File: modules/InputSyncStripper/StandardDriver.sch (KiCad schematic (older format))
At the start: 10 parts

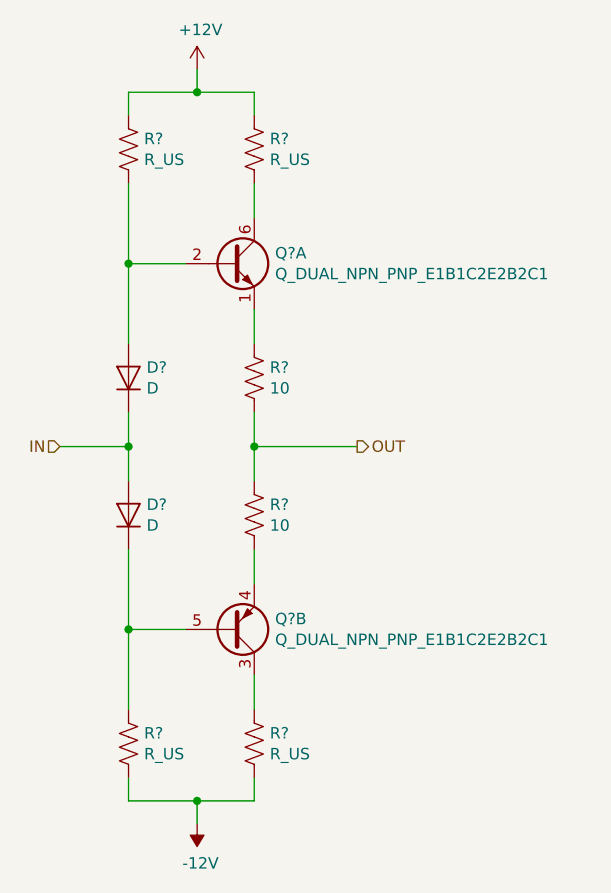
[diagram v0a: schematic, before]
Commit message: fix some ERC issues; assign symbols
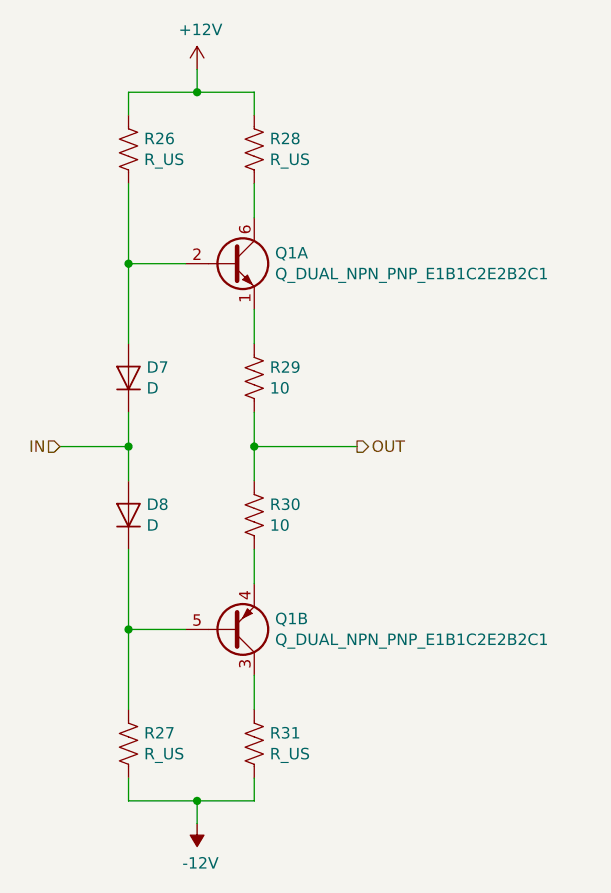
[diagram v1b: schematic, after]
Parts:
- gave numbers to parts that had none: 9
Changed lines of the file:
@@
 EESchema Schematic File Version 4
-LIBS:SIP-cache
+LIBS:InputSyncStripper-cache
 EELAYER 26 0
 EELAYER END
 $Descr A 11000 8500
 encoding utf-8
-Sheet 3 10
+Sheet 9 10
 Title "Sandin Image Processor/Standard Driver"
 Date ""
@@
 OUT
 $Comp
-L Device:D D?
+L Device:D D7
 U 1 1 5BC9A4E0
 P 3950 3450
-AR Path="/5BC7EA60/5BC8D7ED/5BC9A4E0" Ref="D?"  Part="1"
-AR Path="/5BC9C4B4/5BCA0111/5BC9A4E0" Ref="D?"  Part="1"
-AR Path="/5BCA510D/5BCA535E/5BC9A4E0" Ref="D?"  Part="1"
-AR Path="/5BCA5116/5BCAE8EB/5BC9A4E0" Ref="D?"  Part="1"
-F 0 "D?" V 3996 3371 50  0000 R CNN
+AR Path="/5BC7EA60/5BC8D7ED/5BC9A4E0" Ref="D7"  Part="1"
+AR Path="/5BC9C4B4/5BCA0111/5BC9A4E0" Ref="D10"  Part="1"
+AR Path="/5BCA510D/5BCA535E/5BC9A4E0" Ref="D13"  Part="1"
+AR Path="/5BCA5116/5BCAE8EB/5BC9A4E0" Ref="D17"  Part="1"
+F 0 "D7" V 3996 3371 50  0000 R CNN
 F 1 "D" V 3905 3371 50  0000 R CNN
 F 2 "" H 3950 3450 50  0001 C CNN
@@
 $EndComp
 $Comp
-L Device:D D?
+L Device:D D8
 U 1 1 5BC9A54B
 P 3950 4050
-AR Path="/5BC7EA60/5BC8D7ED/5BC9A54B" Ref="D?"  Part="1"
-AR Path="/5BC9C4B4/5BCA0111/5BC9A54B" Ref="D?"  Part="1"
-AR Path="/5BCA510D/5BCA535E/5BC9A54B" Ref="D?"  Part="1"
-AR Path="/5BCA5116/5BCAE8EB/5BC9A54B" Ref="D?"  Part="1"
-F 0 "D?" V 3996 3971 50  0000 R CNN
+AR Path="/5BC7EA60/5BC8D7ED/5BC9A54B" Ref="D8"  Part="1"
+AR Path="/5BC9C4B4/5BCA0111/5BC9A54B" Ref="D11"  Part="1"
+AR Path="/5BCA510D/5BCA535E/5BC9A54B" Ref="D14"  Part="1"
+AR Path="/5BCA5116/5BCAE8EB/5BC9A54B" Ref="D18"  Part="1"
+F 0 "D8" V 3996 3971 50  0000 R CNN
 F 1 "D" V 3905 3971 50  0000 R CNN
 F 2 "" H 3950 4050 50  0001 C CNN
@@
 $EndComp
 $Comp
-L Device:R_US R?
+L Device:R_US R30
 U 1 1 5BC9A59F
 P 4500 4050
-AR Path="/5BC7EA60/5BC8D7ED/5BC9A59F" Ref="R?"  Part="1"
-AR Path="/5BC9C4B4/5BCA0111/5BC9A59F" Ref="R?"  Part="1"
-AR Path="/5BCA510D/5BCA535E/5BC9A59F" Ref="R?"  Part="1"
-AR Path="/5BCA5116/5BCAE8EB/5BC9A59F" Ref="R?"  Part="1"
-F 0 "R?" H 4568 4096 50  0000 L CNN
+AR Path="/5BC7EA60/5BC8D7ED/5BC9A59F" Ref="R30"  Part="1"
+AR Path="/5BC9C4B4/5BCA0111/5BC9A59F" Ref="R41"  Part="1"
+AR Path="/5BCA510D/5BCA535E/5BC9A59F" Ref="R53"  Part="1"
+AR Path="/5BCA5116/5BCAE8EB/5BC9A59F" Ref="R63"  Part="1"
+F 0 "R30" H 4568 4096 50  0000 L CNN
 F 1 "10" H 4568 4005 50  0000 L CNN
 F 2 "" V 4540 4040 50  0001 C CNN
@@
 $EndComp
 $Comp
-L Device:R_US R?
+L Device:R_US R29
 U 1 1 5BC9A608
 P 4500 3450
-AR Path="/5BC7EA60/5BC8D7ED/5BC9A608" Ref="R?"  Part="1"
-AR Path="/5BC9C4B4/5BCA0111/5BC9A608" Ref="R?"  Part="1"
-AR Path="/5BCA510D/5BCA535E/5BC9A608" Ref="R?"  Part="1"
-AR Path="/5BCA5116/5BCAE8EB/5BC9A608" Ref="R?"  Part="1"
-F 0 "R?" H 4568 3496 50  0000 L CNN
+AR Path="/5BC7EA60/5BC8D7ED/5BC9A608" Ref="R29"  Part="1"
+AR Path="/5BC9C4B4/5BCA0111/5BC9A608" Ref="R40"  Part="1"
+AR Path="/5BCA510D/5BCA535E/5BC9A608" Ref="R52"  Part="1"
+AR Path="/5BCA5116/5BCAE8EB/5BC9A608" Ref="R62"  Part="1"
+F 0 "R29" H 4568 3496 50  0000 L CNN
 F 1 "10" H 4568 3405 50  0000 L CNN
 F 2 "" V 4540 3440 50  0001 C CNN
@@
 $EndComp
 $Comp
-L Device:Q_DUAL_NPN_PNP_E1B1C2E2B2C1 Q?
+L Device:Q_DUAL_NPN_PNP_E1B1C2E2B2C1 Q1
 U 1 1 5BC9A901
 P 4400 2950
-AR Path="/5BC7EA60/5BC8D7ED/5BC9A901" Ref="Q?"  Part="1"
-AR Path="/5BC9C4B4/5BCA0111/5BC9A901" Ref="Q?"  Part="1"
-AR Path="/5BCA510D/5BCA535E/5BC9A901" Ref="Q?"  Part="1"
-AR Path="/5BCA5116/5BCAE8EB/5BC9A901" Ref="Q?"  Part="1"
-F 0 "Q?" H 4591 2996 50  0000 L CNN
+AR Path="/5BC7EA60/5BC8D7ED/5BC9A901" Ref="Q1"  Part="1"
+AR Path="/5BC9C4B4/5BCA0111/5BC9A901" Ref="Q2"  Part="1"
+AR Path="/5BCA510D/5BCA535E/5BC9A901" Ref="Q3"  Part="1"
+AR Path="/5BCA5116/5BCAE8EB/5BC9A901" Ref="Q4"  Part="1"
+F 0 "Q1" H 4591 2996 50  0000 L CNN
 F 1 "Q_DUAL_NPN_PNP_E1B1C2E2B2C1" H 4591 2905 50  0000 L CNN
 F 2 "" H 4600 3050 50  0001 C CNN
@@
 $EndComp
 $Comp
-L Device:Q_DUAL_NPN_PNP_E1B1C2E2B2C1 Q?
+L Device:Q_DUAL_NPN_PNP_E1B1C2E2B2C1 Q1
 U 2 1 5BC9A9AF
 P 4400 4550
-AR Path="/5BC7EA60/5BC8D7ED/5BC9A9AF" Ref="Q?"  Part="2"
-AR Path="/5BC9C4B4/5BCA0111/5BC9A9AF" Ref="Q?"  Part="2"
-AR Path="/5BCA510D/5BCA535E/5BC9A9AF" Ref="Q?"  Part="2"
-AR Path="/5BCA5116/5BCAE8EB/5BC9A9AF" Ref="Q?"  Part="2"
-F 0 "Q?" H 4591 4504 50  0000 L CNN
+AR Path="/5BC7EA60/5BC8D7ED/5BC9A9AF" Ref="Q1"  Part="2"
+AR Path="/5BC9C4B4/5BCA0111/5BC9A9AF" Ref="Q2"  Part="2"
+AR Path="/5BCA510D/5BCA535E/5BC9A9AF" Ref="Q3"  Part="2"
+AR Path="/5BCA5116/5BCAE8EB/5BC9A9AF" Ref="Q4"  Part="2"
+F 0 "Q1" H 4591 4504 50  0000 L CNN
 F 1 "Q_DUAL_NPN_PNP_E1B1C2E2B2C1" H 4591 4595 50  0000 L CNN
 F 2 "" H 4600 4650 50  0001 C CNN
@@
 	3950 4550 4200 4550
 $Comp
-L Device:R_US R?
+L Device:R_US R31
 U 1 1 5BC9AC77
 P 4500 5050
-AR Path="/5BC7EA60/5BC8D7ED/5BC9AC77" Ref="R?"  Part="1"
-AR Path="/5BC9C4B4/5BCA0111/5BC9AC77" Ref="R?"  Part="1"
-AR Path="/5BCA510D/5BCA535E/5BC9AC77" Ref="R?"  Part="1"
-AR Path="/5BCA5116/5BCAE8EB/5BC9AC77" Ref="R?"  Part="1"
-F 0 "R?" H 4568 5096 50  0000 L CNN
+AR Path="/5BC7EA60/5BC8D7ED/5BC9AC77" Ref="R31"  Part="1"
+AR Path="/5BC9C4B4/5BCA0111/5BC9AC77" Ref="R42"  Part="1"
+AR Path="/5BCA510D/5BCA535E/5BC9AC77" Ref="R54"  Part="1"
+AR Path="/5BCA5116/5BCAE8EB/5BC9AC77" Ref="R64"  Part="1"
+F 0 "R31" H 4568 5096 50  0000 L CNN
 F 1 "R_US" H 4568 5005 50  0000 L CNN
 F 2 "" V 4540 5040 50  0001 C CNN
@@
 $EndComp
 $Comp
-L Device:R_US R?
+L Device:R_US R28
 U 1 1 5BC9ACDA
 P 4500 2450
-AR Path="/5BC7EA60/5BC8D7ED/5BC9ACDA" Ref="R?"  Part="1"
-AR Path="/5BC9C4B4/5BCA0111/5BC9ACDA" Ref="R?"  Part="1"
-AR Path="/5BCA510D/5BCA535E/5BC9ACDA" Ref="R?"  Part="1"
-AR Path="/5BCA5116/5BCAE8EB/5BC9ACDA" Ref="R?"  Part="1"
-F 0 "R?" H 4568 2496 50  0000 L CNN
+AR Path="/5BC7EA60/5BC8D7ED/5BC9ACDA" Ref="R28"  Part="1"
+AR Path="/5BC9C4B4/5BCA0111/5BC9ACDA" Ref="R39"  Part="1"
+AR Path="/5BCA510D/5BCA535E/5BC9ACDA" Ref="R51"  Part="1"
+AR Path="/5BCA5116/5BCAE8EB/5BC9ACDA" Ref="R61"  Part="1"
+F 0 "R28" H 4568 2496 50  0000 L CNN
 F 1 "R_US" H 4568 2405 50  0000 L CNN
 F 2 "" V 4540 2440 50  0001 C CNN
@@
 $EndComp
 $Comp
-L Device:R_US R?
+L Device:R_US R26
 U 1 1 5BC9AD46
 P 3950 2450
-AR Path="/5BC7EA60/5BC8D7ED/5BC9AD46" Ref="R?"  Part="1"
-AR Path="/5BC9C4B4/5BCA0111/5BC9AD46" Ref="R?"  Part="1"
-AR Path="/5BCA510D/5BCA535E/5BC9AD46" Ref="R?"  Part="1"
-AR Path="/5BCA5116/5BCAE8EB/5BC9AD46" Ref="R?"  Part="1"
-F 0 "R?" H 4018 2496 50  0000 L CNN
+AR Path="/5BC7EA60/5BC8D7ED/5BC9AD46" Ref="R26"  Part="1"
+AR Path="/5BC9C4B4/5BCA0111/5BC9AD46" Ref="R37"  Part="1"
+AR Path="/5BCA510D/5BCA535E/5BC9AD46" Ref="R49"  Part="1"
+AR Path="/5BCA5116/5BCAE8EB/5BC9AD46" Ref="R59"  Part="1"
+F 0 "R26" H 4018 2496 50  0000 L CNN
 F 1 "R_US" H 4018 2405 50  0000 L CNN
 F 2 "" V 3990 2440 50  0001 C CNN
@@
 $EndComp
 $Comp
-L Device:R_US R?
+L Device:R_US R27
 U 1 1 5BC9AD89
 P 3950 5050
-AR Path="/5BC7EA60/5BC8D7ED/5BC9AD89" Ref="R?"  Part="1"
-AR Path="/5BC9C4B4/5BCA0111/5BC9AD89" Ref="R?"  Part="1"
-AR Path="/5BCA510D/5BCA535E/5BC9AD89" Ref="R?"  Part="1"
-AR Path="/5BCA5116/5BCAE8EB/5BC9AD89" Ref="R?"  Part="1"
-F 0 "R?" H 4018 5096 50  0000 L CNN
+AR Path="/5BC7EA60/5BC8D7ED/5BC9AD89" Ref="R27"  Part="1"
+AR Path="/5BC9C4B4/5BCA0111/5BC9AD89" Ref="R38"  Part="1"
+AR Path="/5BCA510D/5BCA535E/5BC9AD89" Ref="R50"  Part="1"
+AR Path="/5BCA5116/5BCAE8EB/5BC9AD89" Ref="R60"  Part="1"
+F 0 "R27" H 4018 5096 50  0000 L CNN
 F 1 "R_US" H 4018 5005 50  0000 L CNN
 F 2 "" V 3990 5040 50  0001 C CNN
@@
 $EndComp
 $Comp
-L power:+12V #PWR?
+L power:+12V #PWR012
 U 1 1 5BC9AED2
 P 4250 2100
-AR Path="/5BC7EA60/5BC8D7ED/5BC9AED2" Ref="#PWR?"  Part="1"
-AR Path="/5BC9C4B4/5BCA0111/5BC9AED2" Ref="#PWR?"  Part="1"
-AR Path="/5BCA510D/5BCA535E/5BC9AED2" Ref="#PWR?"  Part="1"
-AR Path="/5BCA5116/5BCAE8EB/5BC9AED2" Ref="#PWR?"  Part="1"
-F 0 "#PWR?" H 4250 1950 50  0001 C CNN
+AR Path="/5BC7EA60/5BC8D7ED/5BC9AED2" Ref="#PWR012"  Part="1"
+AR Path="/5BC9C4B4/5BCA0111/5BC9AED2" Ref="#PWR018"  Part="1"
+AR Path="/5BCA510D/5BCA535E/5BC9AED2" Ref="#PWR024"  Part="1"
+AR Path="/5BCA5116/5BCAE8EB/5BC9AED2" Ref="#PWR029"  Part="1"
+F 0 "#PWR029" H 4250 1950 50  0001 C CNN
 F 1 "+12V" H 4265 2273 50  0000 C CNN
 F 2 "" H 4250 2100 50  0001 C CNN
@@
 $EndComp
 $Comp
-L power:-12V #PWR?
+L power:-12V #PWR013
 U 1 1 5BC9AF87
 P 4250 5400
-AR Path="/5BC7EA60/5BC8D7ED/5BC9AF87" Ref="#PWR?"  Part="1"
-AR Path="/5BC9C4B4/5BCA0111/5BC9AF87" Ref="#PWR?"  Part="1"
-AR Path="/5BCA510D/5BCA535E/5BC9AF87" Ref="#PWR?"  Part="1"
-AR Path="/5BCA5116/5BCAE8EB/5BC9AF87" Ref="#PWR?"  Part="1"
-F 0 "#PWR?" H 4250 5500 50  0001 C CNN
+AR Path="/5BC7EA60/5BC8D7ED/5BC9AF87" Ref="#PWR013"  Part="1"
+AR Path="/5BC9C4B4/5BCA0111/5BC9AF87" Ref="#PWR019"  Part="1"
+AR Path="/5BCA510D/5BCA535E/5BC9AF87" Ref="#PWR025"  Part="1"
+AR Path="/5BCA5116/5BCAE8EB/5BC9AF87" Ref="#PWR030"  Part="1"
+F 0 "#PWR030" H 4250 5500 50  0001 C CNN
 F 1 "-12V" H 4265 5573 50  0000 C CNN
 F 2 "" H 4250 5400 50  0001 C CNN

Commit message: added power pins for opamps and tied inputs of unused amp
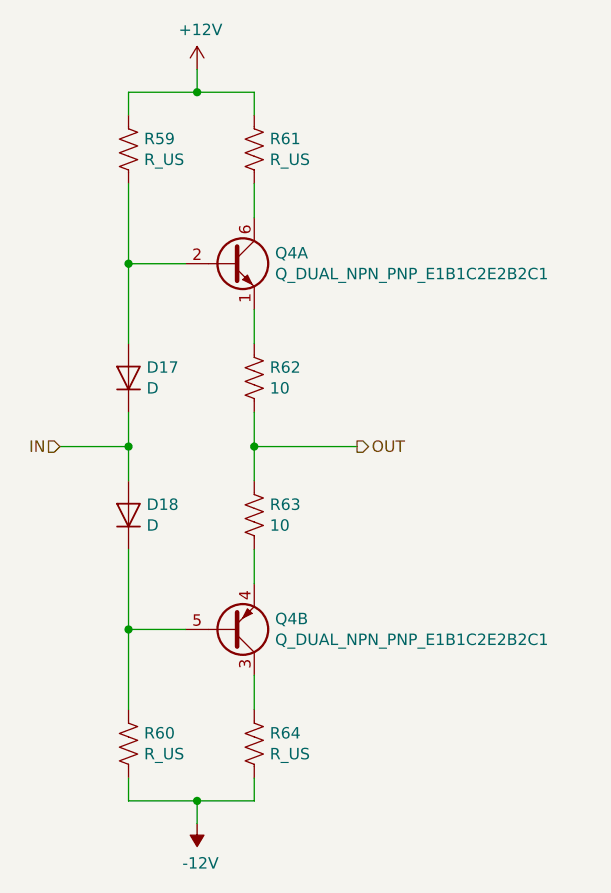
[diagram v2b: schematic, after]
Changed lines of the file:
@@
 AR Path="/5BCA510D/5BCA535E/5BC9A4E0" Ref="D13"  Part="1"
 AR Path="/5BCA5116/5BCAE8EB/5BC9A4E0" Ref="D17"  Part="1"
-F 0 "D7" V 3996 3371 50  0000 R CNN
+F 0 "D17" V 3996 3371 50  0000 R CNN
 F 1 "D" V 3905 3371 50  0000 R CNN
 F 2 "" H 3950 3450 50  0001 C CNN
@@
 AR Path="/5BCA510D/5BCA535E/5BC9A54B" Ref="D14"  Part="1"
 AR Path="/5BCA5116/5BCAE8EB/5BC9A54B" Ref="D18"  Part="1"
-F 0 "D8" V 3996 3971 50  0000 R CNN
+F 0 "D18" V 3996 3971 50  0000 R CNN
 F 1 "D" V 3905 3971 50  0000 R CNN
 F 2 "" H 3950 4050 50  0001 C CNN
@@
 AR Path="/5BCA510D/5BCA535E/5BC9A59F" Ref="R53"  Part="1"
 AR Path="/5BCA5116/5BCAE8EB/5BC9A59F" Ref="R63"  Part="1"
-F 0 "R30" H 4568 4096 50  0000 L CNN
+F 0 "R63" H 4568 4096 50  0000 L CNN
 F 1 "10" H 4568 4005 50  0000 L CNN
 F 2 "" V 4540 4040 50  0001 C CNN
@@
 AR Path="/5BCA510D/5BCA535E/5BC9A608" Ref="R52"  Part="1"
 AR Path="/5BCA5116/5BCAE8EB/5BC9A608" Ref="R62"  Part="1"
-F 0 "R29" H 4568 3496 50  0000 L CNN
+F 0 "R62" H 4568 3496 50  0000 L CNN
 F 1 "10" H 4568 3405 50  0000 L CNN
 F 2 "" V 4540 3440 50  0001 C CNN
@@
 AR Path="/5BCA510D/5BCA535E/5BC9A901" Ref="Q3"  Part="1"
 AR Path="/5BCA5116/5BCAE8EB/5BC9A901" Ref="Q4"  Part="1"
-F 0 "Q1" H 4591 2996 50  0000 L CNN
+F 0 "Q4" H 4591 2996 50  0000 L CNN
 F 1 "Q_DUAL_NPN_PNP_E1B1C2E2B2C1" H 4591 2905 50  0000 L CNN
 F 2 "" H 4600 3050 50  0001 C CNN
@@
 AR Path="/5BCA510D/5BCA535E/5BC9A9AF" Ref="Q3"  Part="2"
 AR Path="/5BCA5116/5BCAE8EB/5BC9A9AF" Ref="Q4"  Part="2"
-F 0 "Q1" H 4591 4504 50  0000 L CNN
+F 0 "Q4" H 4591 4504 50  0000 L CNN
 F 1 "Q_DUAL_NPN_PNP_E1B1C2E2B2C1" H 4591 4595 50  0000 L CNN
 F 2 "" H 4600 4650 50  0001 C CNN
@@
 AR Path="/5BCA510D/5BCA535E/5BC9AC77" Ref="R54"  Part="1"
 AR Path="/5BCA5116/5BCAE8EB/5BC9AC77" Ref="R64"  Part="1"
-F 0 "R31" H 4568 5096 50  0000 L CNN
+F 0 "R64" H 4568 5096 50  0000 L CNN
 F 1 "R_US" H 4568 5005 50  0000 L CNN
 F 2 "" V 4540 5040 50  0001 C CNN
@@
 AR Path="/5BCA510D/5BCA535E/5BC9ACDA" Ref="R51"  Part="1"
 AR Path="/5BCA5116/5BCAE8EB/5BC9ACDA" Ref="R61"  Part="1"
-F 0 "R28" H 4568 2496 50  0000 L CNN
+F 0 "R61" H 4568 2496 50  0000 L CNN
 F 1 "R_US" H 4568 2405 50  0000 L CNN
 F 2 "" V 4540 2440 50  0001 C CNN
@@
 AR Path="/5BCA510D/5BCA535E/5BC9AD46" Ref="R49"  Part="1"
 AR Path="/5BCA5116/5BCAE8EB/5BC9AD46" Ref="R59"  Part="1"
-F 0 "R26" H 4018 2496 50  0000 L CNN
+F 0 "R59" H 4018 2496 50  0000 L CNN
 F 1 "R_US" H 4018 2405 50  0000 L CNN
 F 2 "" V 3990 2440 50  0001 C CNN
@@
 AR Path="/5BCA510D/5BCA535E/5BC9AD89" Ref="R50"  Part="1"
 AR Path="/5BCA5116/5BCAE8EB/5BC9AD89" Ref="R60"  Part="1"
-F 0 "R27" H 4018 5096 50  0000 L CNN
+F 0 "R60" H 4018 5096 50  0000 L CNN
 F 1 "R_US" H 4018 5005 50  0000 L CNN
 F 2 "" V 3990 5040 50  0001 C CNN

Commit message: Find and fix missing values
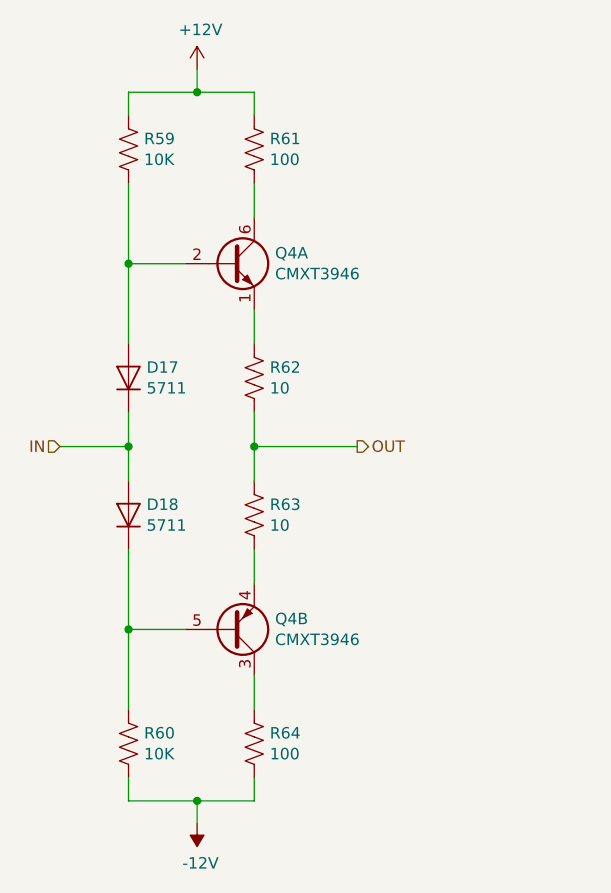
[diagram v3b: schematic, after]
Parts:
- D7, D8: value D -> 5711
- Q1: value Q_DUAL_NPN_PNP_E1B1C2E2B2C1 -> CMXT3946
- R26, R27: value R_US -> 10K
- R28, R31: value R_US -> 100
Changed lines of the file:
@@
 AR Path="/5BCA5116/5BCAE8EB/5BC9A4E0" Ref="D17"  Part="1"
 F 0 "D17" V 3996 3371 50  0000 R CNN
-F 1 "D" V 3905 3371 50  0000 R CNN
+F 1 "5711" V 3905 3371 50  0000 R CNN
 F 2 "" H 3950 3450 50  0001 C CNN
 F 3 "~" H 3950 3450 50  0001 C CNN
@@
 AR Path="/5BCA5116/5BCAE8EB/5BC9A54B" Ref="D18"  Part="1"
 F 0 "D18" V 3996 3971 50  0000 R CNN
-F 1 "D" V 3905 3971 50  0000 R CNN
+F 1 "5711" V 3905 3971 50  0000 R CNN
 F 2 "" H 3950 4050 50  0001 C CNN
 F 3 "~" H 3950 4050 50  0001 C CNN
@@
 AR Path="/5BCA5116/5BCAE8EB/5BC9A901" Ref="Q4"  Part="1"
 F 0 "Q4" H 4591 2996 50  0000 L CNN
-F 1 "Q_DUAL_NPN_PNP_E1B1C2E2B2C1" H 4591 2905 50  0000 L CNN
+F 1 "CMXT3946" H 4591 2905 50  0000 L CNN
 F 2 "" H 4600 3050 50  0001 C CNN
 F 3 "~" H 4400 2950 50  0001 C CNN
@@
 AR Path="/5BCA5116/5BCAE8EB/5BC9A9AF" Ref="Q4"  Part="2"
 F 0 "Q4" H 4591 4504 50  0000 L CNN
-F 1 "Q_DUAL_NPN_PNP_E1B1C2E2B2C1" H 4591 4595 50  0000 L CNN
+F 1 "CMXT3946" H 4591 4595 50  0000 L CNN
 F 2 "" H 4600 4650 50  0001 C CNN
 F 3 "~" H 4400 4550 50  0001 C CNN
@@
 AR Path="/5BCA5116/5BCAE8EB/5BC9AC77" Ref="R64"  Part="1"
 F 0 "R64" H 4568 5096 50  0000 L CNN
-F 1 "R_US" H 4568 5005 50  0000 L CNN
+F 1 "100" H 4568 5005 50  0000 L CNN
 F 2 "" V 4540 5040 50  0001 C CNN
 F 3 "~" H 4500 5050 50  0001 C CNN
@@
 AR Path="/5BCA5116/5BCAE8EB/5BC9ACDA" Ref="R61"  Part="1"
 F 0 "R61" H 4568 2496 50  0000 L CNN
-F 1 "R_US" H 4568 2405 50  0000 L CNN
+F 1 "100" H 4568 2405 50  0000 L CNN
 F 2 "" V 4540 2440 50  0001 C CNN
 F 3 "~" H 4500 2450 50  0001 C CNN
@@
 AR Path="/5BCA5116/5BCAE8EB/5BC9AD46" Ref="R59"  Part="1"
 F 0 "R59" H 4018 2496 50  0000 L CNN
-F 1 "R_US" H 4018 2405 50  0000 L CNN
+F 1 "10K" H 4018 2405 50  0000 L CNN
 F 2 "" V 3990 2440 50  0001 C CNN
 F 3 "~" H 3950 2450 50  0001 C CNN
@@
 AR Path="/5BCA5116/5BCAE8EB/5BC9AD89" Ref="R60"  Part="1"
 F 0 "R60" H 4018 5096 50  0000 L CNN
-F 1 "R_US" H 4018 5005 50  0000 L CNN
+F 1 "10K" H 4018 5005 50  0000 L CNN
 F 2 "" V 3990 5040 50  0001 C CNN
 F 3 "~" H 3950 5050 50  0001 C CNN

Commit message: building out footprints/BOM
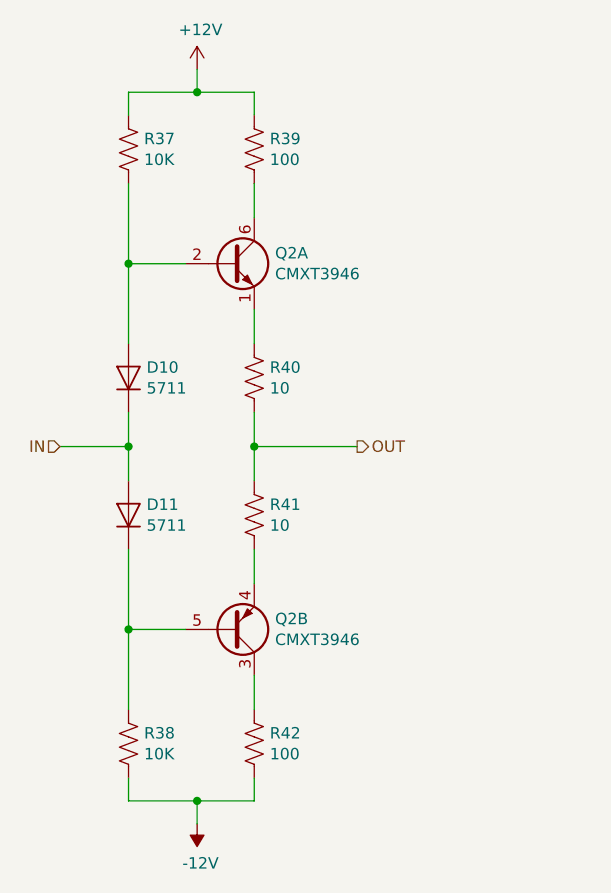
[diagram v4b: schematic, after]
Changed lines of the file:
@@
 AR Path="/5BCA510D/5BCA535E/5BC9A4E0" Ref="D13"  Part="1"
 AR Path="/5BCA5116/5BCAE8EB/5BC9A4E0" Ref="D17"  Part="1"
-F 0 "D17" V 3996 3371 50  0000 R CNN
+F 0 "D10" V 3996 3371 50  0000 R CNN
 F 1 "5711" V 3905 3371 50  0000 R CNN
 F 2 "" H 3950 3450 50  0001 C CNN
@@
 AR Path="/5BCA510D/5BCA535E/5BC9A54B" Ref="D14"  Part="1"
 AR Path="/5BCA5116/5BCAE8EB/5BC9A54B" Ref="D18"  Part="1"
-F 0 "D18" V 3996 3971 50  0000 R CNN
+F 0 "D11" V 3996 3971 50  0000 R CNN
 F 1 "5711" V 3905 3971 50  0000 R CNN
 F 2 "" H 3950 4050 50  0001 C CNN
@@
 AR Path="/5BCA510D/5BCA535E/5BC9A59F" Ref="R53"  Part="1"
 AR Path="/5BCA5116/5BCAE8EB/5BC9A59F" Ref="R63"  Part="1"
-F 0 "R63" H 4568 4096 50  0000 L CNN
+F 0 "R41" H 4568 4096 50  0000 L CNN
 F 1 "10" H 4568 4005 50  0000 L CNN
 F 2 "" V 4540 4040 50  0001 C CNN
@@
 AR Path="/5BCA510D/5BCA535E/5BC9A608" Ref="R52"  Part="1"
 AR Path="/5BCA5116/5BCAE8EB/5BC9A608" Ref="R62"  Part="1"
-F 0 "R62" H 4568 3496 50  0000 L CNN
+F 0 "R40" H 4568 3496 50  0000 L CNN
 F 1 "10" H 4568 3405 50  0000 L CNN
 F 2 "" V 4540 3440 50  0001 C CNN
@@
 AR Path="/5BCA510D/5BCA535E/5BC9A901" Ref="Q3"  Part="1"
 AR Path="/5BCA5116/5BCAE8EB/5BC9A901" Ref="Q4"  Part="1"
-F 0 "Q4" H 4591 2996 50  0000 L CNN
+F 0 "Q2" H 4591 2996 50  0000 L CNN
 F 1 "CMXT3946" H 4591 2905 50  0000 L CNN
 F 2 "" H 4600 3050 50  0001 C CNN
@@
 AR Path="/5BCA510D/5BCA535E/5BC9A9AF" Ref="Q3"  Part="2"
 AR Path="/5BCA5116/5BCAE8EB/5BC9A9AF" Ref="Q4"  Part="2"
-F 0 "Q4" H 4591 4504 50  0000 L CNN
+F 0 "Q2" H 4591 4504 50  0000 L CNN
 F 1 "CMXT3946" H 4591 4595 50  0000 L CNN
 F 2 "" H 4600 4650 50  0001 C CNN
@@
 AR Path="/5BCA510D/5BCA535E/5BC9AC77" Ref="R54"  Part="1"
 AR Path="/5BCA5116/5BCAE8EB/5BC9AC77" Ref="R64"  Part="1"
-F 0 "R64" H 4568 5096 50  0000 L CNN
+F 0 "R42" H 4568 5096 50  0000 L CNN
 F 1 "100" H 4568 5005 50  0000 L CNN
 F 2 "" V 4540 5040 50  0001 C CNN
@@
 AR Path="/5BCA510D/5BCA535E/5BC9ACDA" Ref="R51"  Part="1"
 AR Path="/5BCA5116/5BCAE8EB/5BC9ACDA" Ref="R61"  Part="1"
-F 0 "R61" H 4568 2496 50  0000 L CNN
+F 0 "R39" H 4568 2496 50  0000 L CNN
 F 1 "100" H 4568 2405 50  0000 L CNN
 F 2 "" V 4540 2440 50  0001 C CNN
@@
 AR Path="/5BCA510D/5BCA535E/5BC9AD46" Ref="R49"  Part="1"
 AR Path="/5BCA5116/5BCAE8EB/5BC9AD46" Ref="R59"  Part="1"
-F 0 "R59" H 4018 2496 50  0000 L CNN
+F 0 "R37" H 4018 2496 50  0000 L CNN
 F 1 "10K" H 4018 2405 50  0000 L CNN
 F 2 "" V 3990 2440 50  0001 C CNN
@@
 AR Path="/5BCA510D/5BCA535E/5BC9AD89" Ref="R50"  Part="1"
 AR Path="/5BCA5116/5BCAE8EB/5BC9AD89" Ref="R60"  Part="1"
-F 0 "R60" H 4018 5096 50  0000 L CNN
+F 0 "R38" H 4018 5096 50  0000 L CNN
 F 1 "10K" H 4018 5005 50  0000 L CNN
 F 2 "" V 3990 5040 50  0001 C CNN
@@
 AR Path="/5BCA510D/5BCA535E/5BC9AED2" Ref="#PWR024"  Part="1"
 AR Path="/5BCA5116/5BCAE8EB/5BC9AED2" Ref="#PWR029"  Part="1"
-F 0 "#PWR029" H 4250 1950 50  0001 C CNN
+F 0 "#PWR018" H 4250 1950 50  0001 C CNN
 F 1 "+12V" H 4265 2273 50  0000 C CNN
 F 2 "" H 4250 2100 50  0001 C CNN
@@
 AR Path="/5BCA510D/5BCA535E/5BC9AF87" Ref="#PWR025"  Part="1"
 AR Path="/5BCA5116/5BCAE8EB/5BC9AF87" Ref="#PWR030"  Part="1"
-F 0 "#PWR030" H 4250 5500 50  0001 C CNN
+F 0 "#PWR019" H 4250 5500 50  0001 C CNN
 F 1 "-12V" H 4265 5573 50  0000 C CNN
 F 2 "" H 4250 5400 50  0001 C CNN
